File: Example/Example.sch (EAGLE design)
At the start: 24 parts, among them IC2 74LS02D, IC3 74LS02D, U1 CD4017

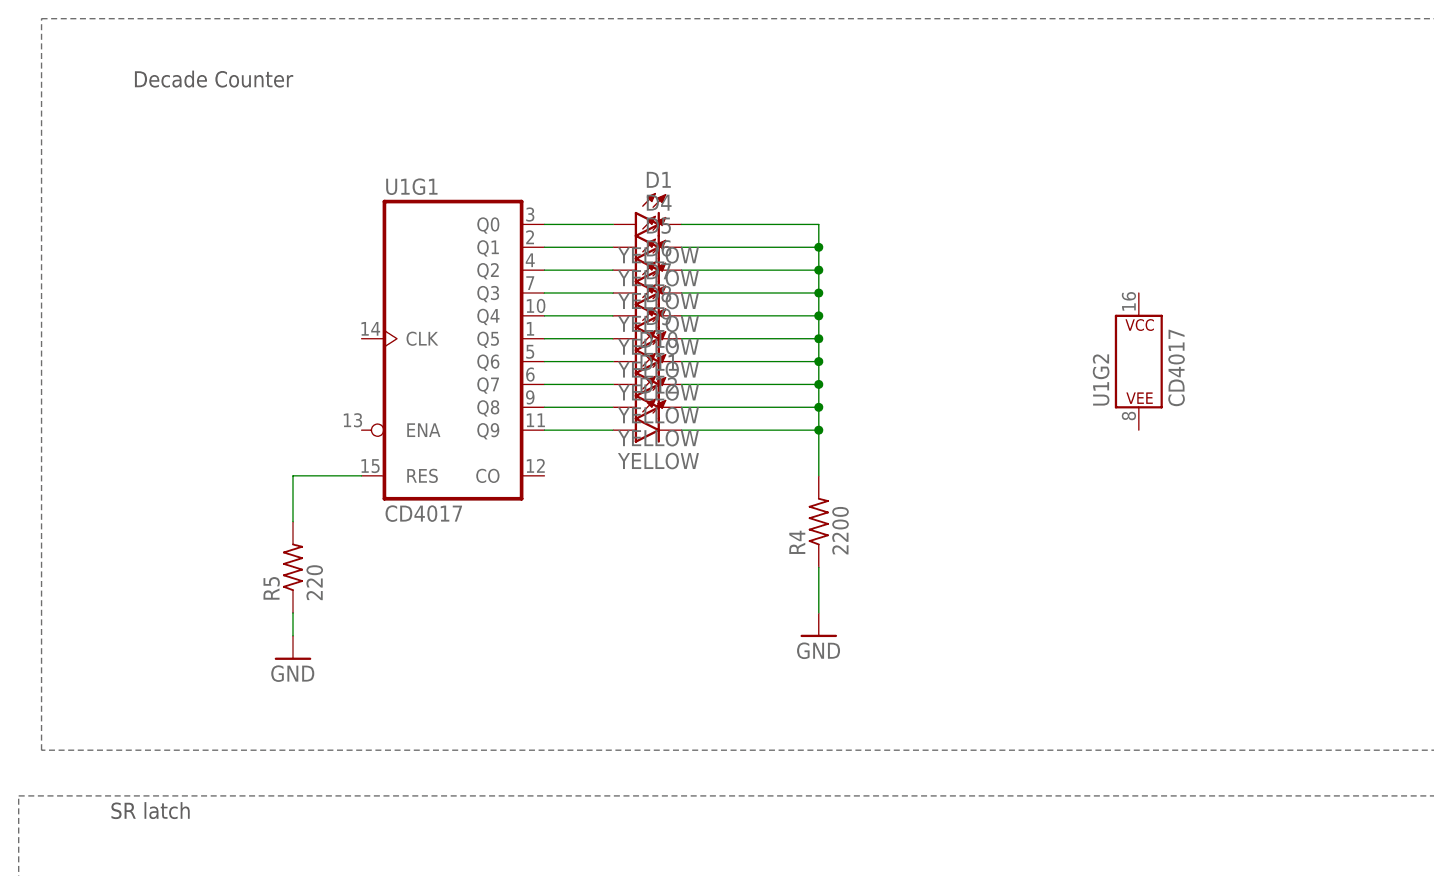
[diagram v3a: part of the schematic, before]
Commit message: decade counter
added clocks and EN
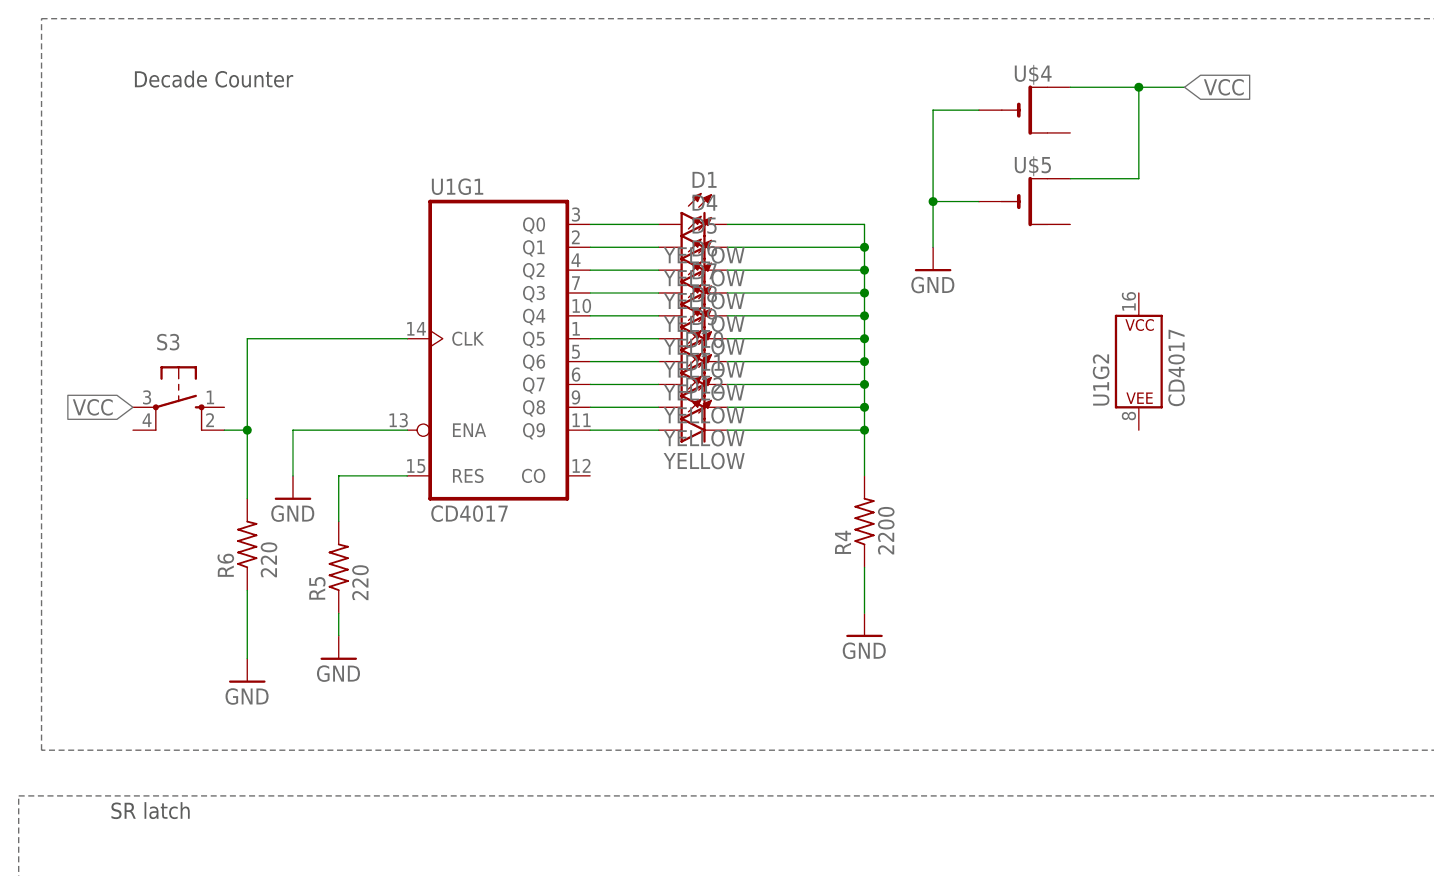
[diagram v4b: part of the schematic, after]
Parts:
- added R6: 220, rcl:R-US_R0603
- added S3: (no value), adafruit:40-XX-ROUND
- added U$4, U$5: (no value), adafruit:CR1220SMT
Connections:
- new net N$1: R6.2, S3.S1, U1G1.CLK
- net GND: now also R6.1, U$4.-, U$5.-, U1G1.ENA
- net VCC: now also U$4.+, U$5.+
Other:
- moved on the sheet: D1, D10, D11, D12, D4, D5, D6, D7, D8, D9, R4, R5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
